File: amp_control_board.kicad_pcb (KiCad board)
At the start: 2 copper layers, 100.1 x 61 mm, 79 parts, among them J1 Conn_01x03_Male, J2 Conn_01x04_Female, J3 Conn_01x03_Male, J4 Screw_Terminal_01x02, J5 Conn_01x04_Female, J6 Conn_02x03_Odd_Even, J7 Conn_01x03_Male, M1 Fan_4pin, M2 Fan_4pin, Q1 BSP89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

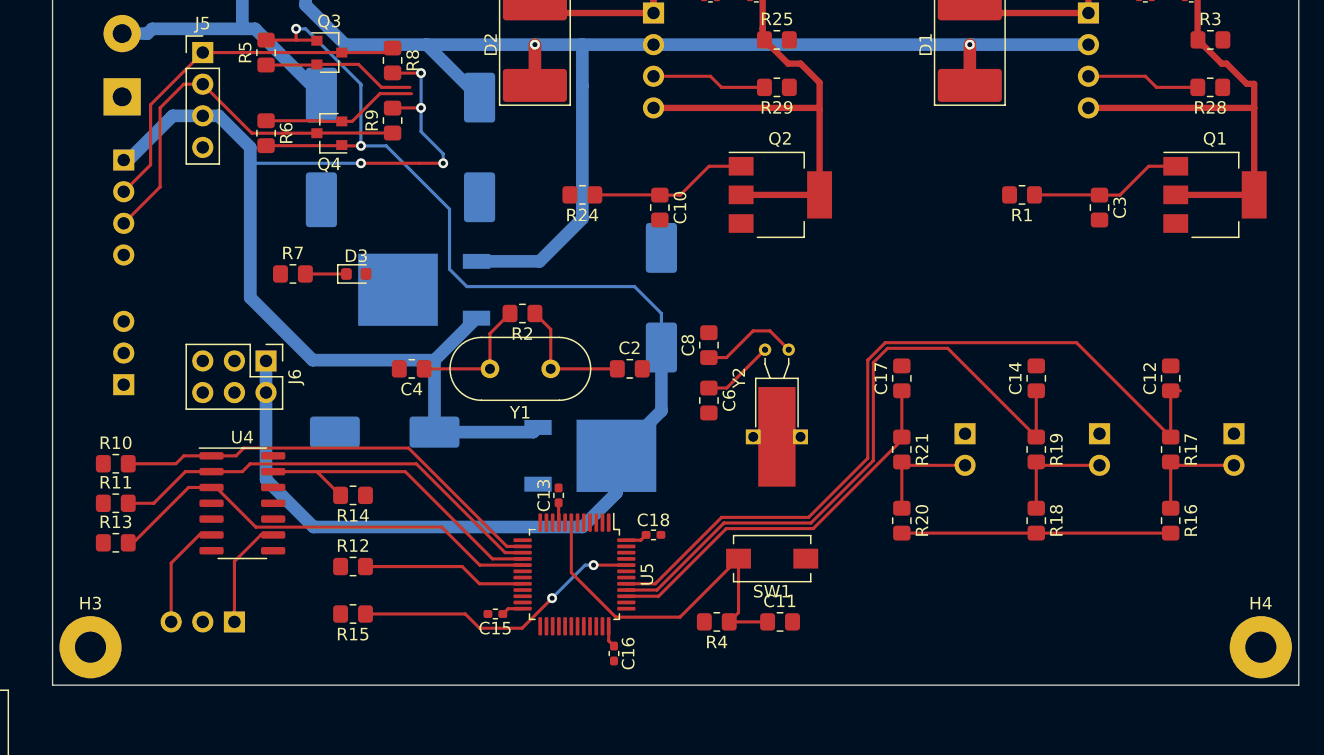
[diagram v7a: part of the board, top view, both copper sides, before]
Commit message: routed some more on top layer, added USB interface
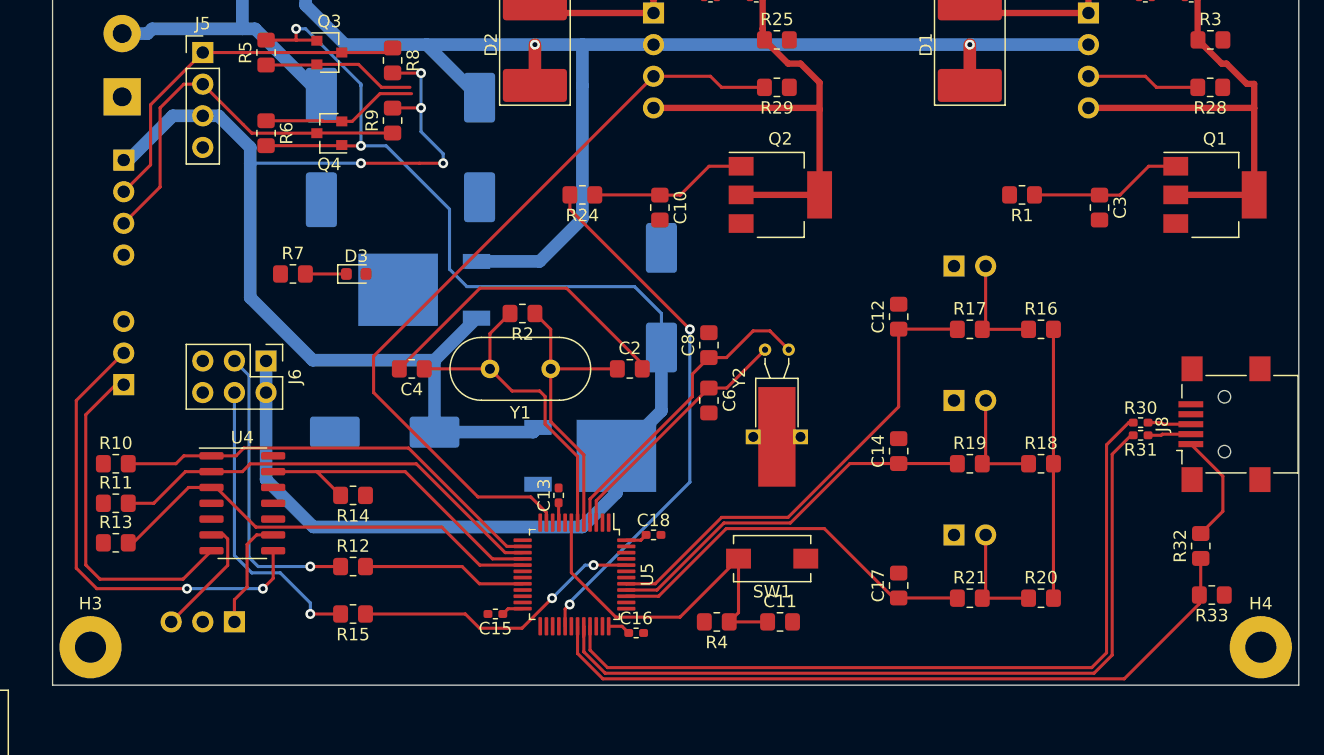
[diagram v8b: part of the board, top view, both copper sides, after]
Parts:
- added J8: USB_B_Mini, Connector_USB:USB_Mini-B_Lumberg_2486_01_Horizontal, F.Cu at (221.1, 106.0)
- added R30: 20R, Resistor_SMD:R_0402_1005Metric_Pad0.72x0.64mm_HandSolder, F.Cu at (214.4, 105.9)
- added R31: 20R, Resistor_SMD:R_0402_1005Metric_Pad0.72x0.64mm_HandSolder, F.Cu at (214.4, 106.9)
- added R32: 4K7, Resistor_SMD:R_0805_2012Metric_Pad1.20x1.40mm_HandSolder, F.Cu at (219.2, 115.8)
- added R33: 9K1, Resistor_SMD:R_0805_2012Metric_Pad1.20x1.40mm_HandSolder, F.Cu at (220.1, 119.8)
- moved SW2 26.2 mm to (199.4, 93.3), turned to 270 degrees
- moved C12 22.4 mm to (194.9, 97.4)
- moved R17 18.8 mm to (200.7, 98.4), turned to 0 degrees
- moved R16 18.6 mm to (206.4, 98.4), turned to 0 degrees
- moved C17 16.6 mm to (194.9, 119.0)
- moved R21 13.1 mm to (200.7, 120.0), turned to 0 degrees
- moved R20 12.8 mm to (206.4, 120.0), turned to 0 degrees
- moved C14 12.5 mm to (194.9, 108.2)
- moved SW3 12.0 mm to (199.4, 104.1), turned to 270 degrees
- moved SW4 8.18 mm to (199.4, 114.9), turned to 270 degrees
- moved R19 5.46 mm to (200.7, 109.2), turned to 0 degrees
- moved R18 4.59 mm to (206.4, 109.2), turned to 0 degrees
- moved C16 2.43 mm to (173.9, 122.8), turned to 0 degrees
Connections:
- U5 pad 31: Net-(U5-Pad31) -> USB_DT
- U5 pad 32: Net-(U5-Pad32) -> USB_M
- U5 pad 33: Net-(U5-Pad33) -> USB_P
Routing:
- net USB_M: track 0.00 -> 65.1 mm
- net USB_P: track 0.00 -> 64.0 mm
- net USB_DT: track 0.00 -> 59.1 mm
- net TIM2_CH2: track 9.27 -> 62.7 mm
- net TIM1_CH1: track 0.00 -> 42.8 mm, vias 0 -> 2
- net AUDIO_IN_R: track 0.00 -> 37.9 mm, vias 0 -> 2
- net AUDIO_IN_L: track 0.00 -> 27.6 mm
- net BTN_MODE: track 64.0 -> 38.8 mm
- net Net-(C2-Pad2): track 0.00 -> 25.1 mm
- net Net-(J6-Pad4): track 0.00 -> 24.1 mm, vias 0 -> 1
- net Net-(J6-Pad3): track 0.00 -> 23.9 mm, vias 0 -> 1
- net BTN_UP: track 52.3 -> 30.8 mm
- net LSE_OSC2: track 7.92 -> 25.1 mm
- net OSCOUT: track 10.4 -> 26.9 mm
- net LSE_OSC1: track 5.79 -> 20.3 mm
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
